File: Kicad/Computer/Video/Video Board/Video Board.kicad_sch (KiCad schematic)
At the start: 34 parts, among them IC1 74LVC2G04GW-Q100H, IC1 AP7365-33WG-7, IC1 SST39VF010-70-4I-NHE, IC27 74LVC1GX04GW,125, IC3 LD1117S50C

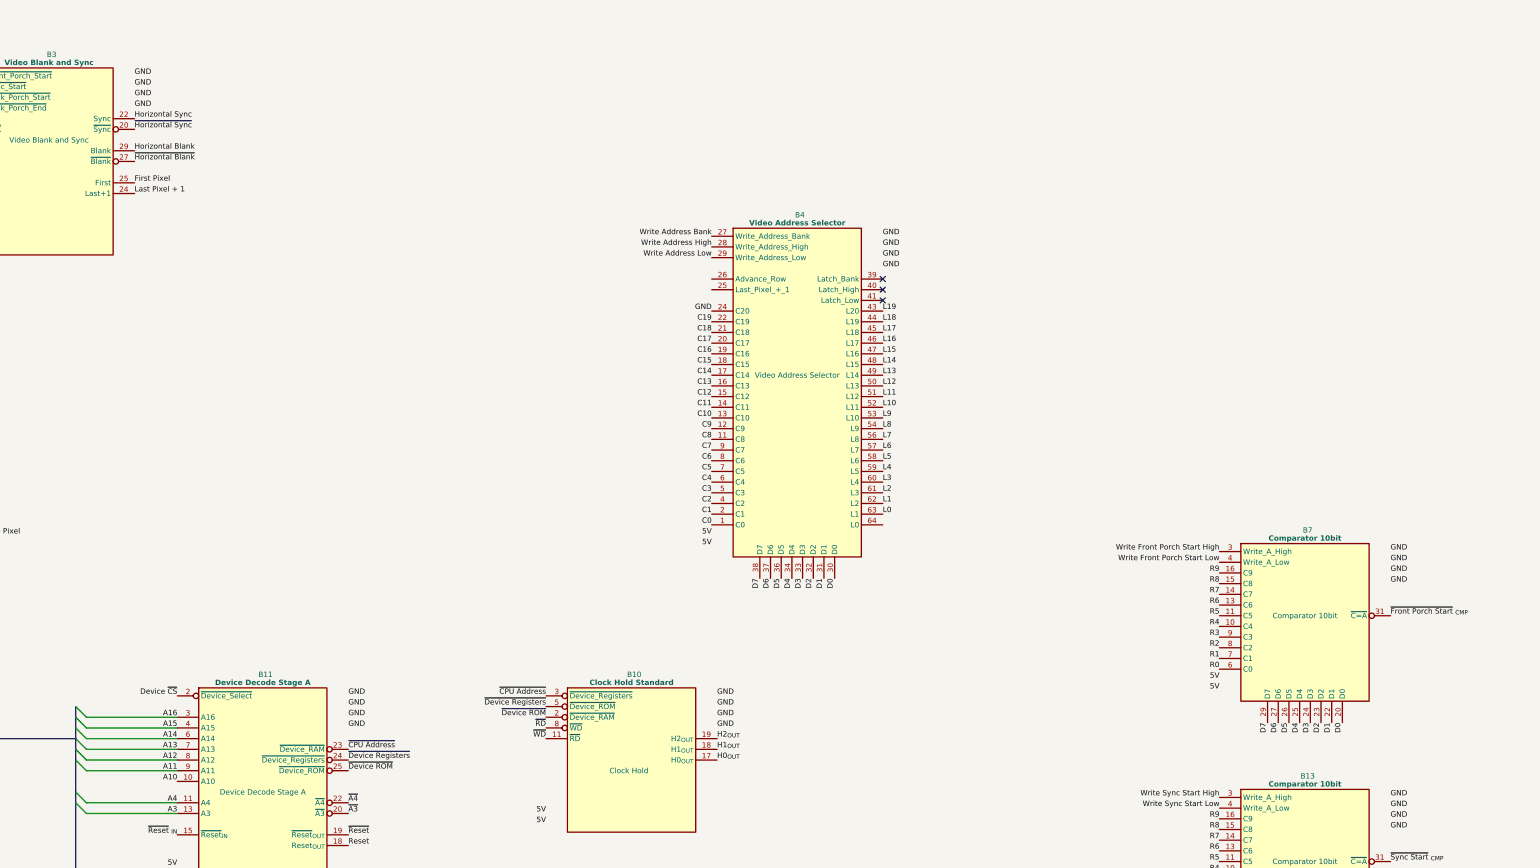
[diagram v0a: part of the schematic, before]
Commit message: Added Video Address Reader schematic and PCB.
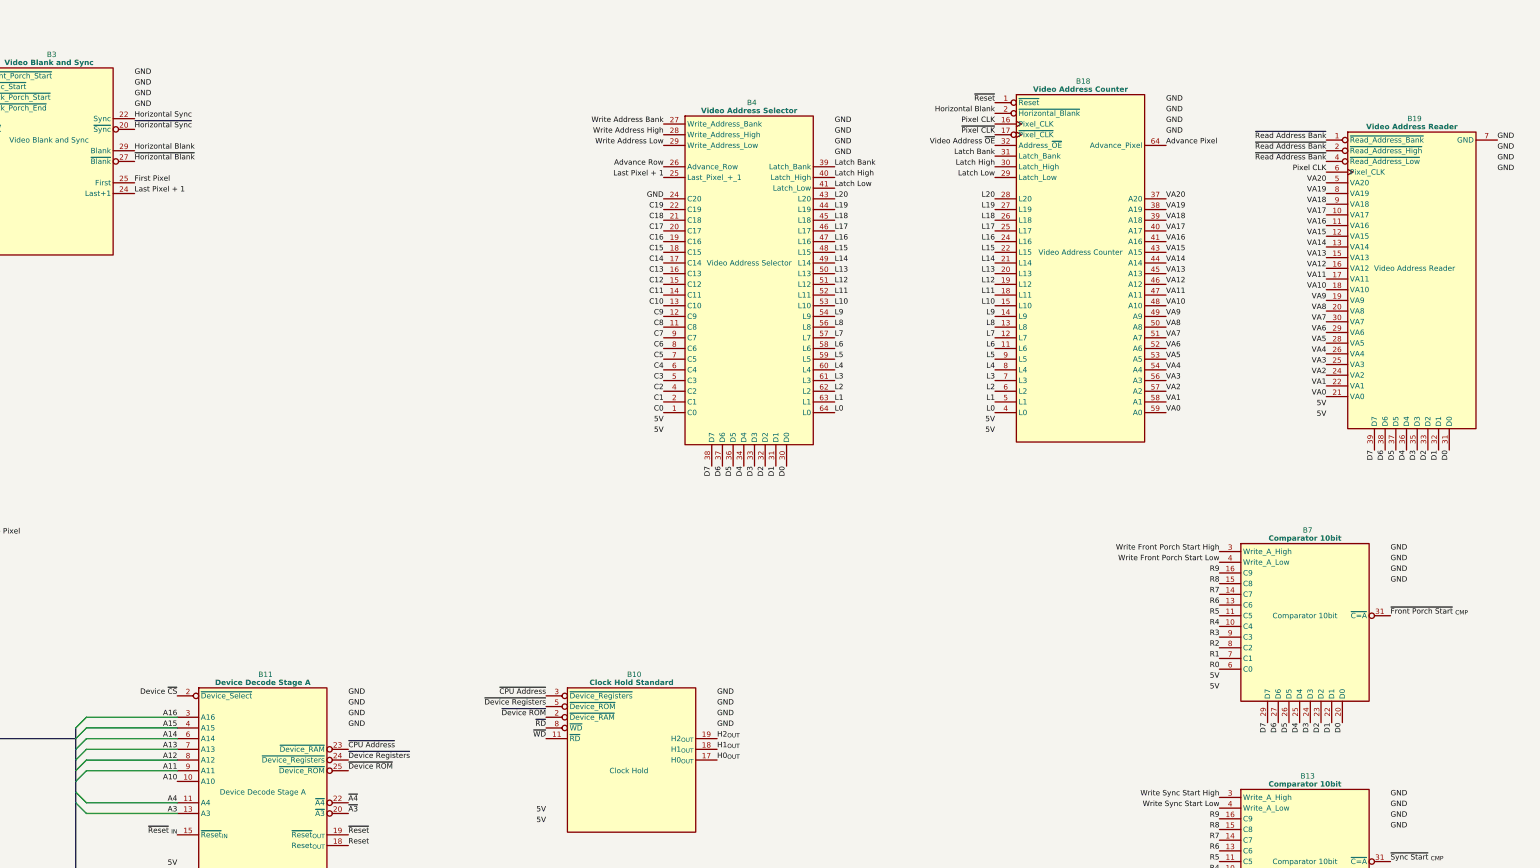
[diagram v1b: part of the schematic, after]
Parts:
- added B18: Video Address Counter, HCP65_Parts:HCP65_Video_Address_Counter, symbol HCP65:Video_Address_Counter
- added B19: Video Address Reader, HCP65_Parts:HCP65_Video_Address_Reader, symbol HCP65:Video_Address_Reader
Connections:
- net 5V: now also B18.3 (5V), B18.35 (5V), B19.23 (5V), B19.3 (5V)
- net Advance Pixel: now also B18.64 (Advance_Pixel)
- net D0: now also B19.31 (D0)
- net D1: now also B19.32 (D1)
- net D2: now also B19.33 (D2)
- net D3: now also B19.35 (D3)
- net D4: now also B19.36 (D4)
- net D5: now also B19.37 (D5)
- net D6: now also B19.38 (D6)
- net D7: now also B19.39 (D7)
- net GND: now also B18.10 (GND), B18.23 (GND), B18.42 (GND), B18.55 (GND), B19.14 (GND), B19.27 (GND), B19.34 (GND), B19.7 (GND)
- net Horizontal Blank: now also B18.2 (~{Horizontal_Blank})
- net L0: now also B4.64 (L0), B18.4 (L0); no longer B4.63 (L1)
- net L1: now also B4.63 (L1), B18.5 (L1); no longer B4.62 (L2)
- net L10: now also B4.53 (L10), B18.15 (L10); no longer B4.52 (L11)
- net L11: now also B4.52 (L11), B18.18 (L11); no longer B4.51 (L12)
- net L12: now also B4.51 (L12), B18.19 (L12); no longer B4.50 (L13)
- net L13: now also B4.50 (L13), B18.20 (L13); no longer B4.49 (L14)
- net L14: now also B4.49 (L14), B18.21 (L14); no longer B4.48 (L15)
- net L15: now also B4.48 (L15), B18.22 (L15); no longer B4.47 (L16)
- net L16: now also B4.47 (L16), B18.24 (L16); no longer B4.46 (L17)
- net L17: now also B4.46 (L17), B18.25 (L17); no longer B4.45 (L18)
- net L18: now also B4.45 (L18), B18.26 (L18); no longer B4.44 (L19)
- net L19: now also B4.44 (L19), B18.27 (L19); no longer B4.43 (L20)
- net L2: now also B4.62 (L2), B18.6 (L2); no longer B4.61 (L3)
- net L3: now also B4.61 (L3), B18.7 (L3); no longer B4.60 (L4)
- net L4: now also B4.60 (L4), B18.8 (L4); no longer B4.59 (L5)
- net L5: now also B4.59 (L5), B18.9 (L5); no longer B4.58 (L6)
- net L6: now also B4.58 (L6), B18.11 (L6); no longer B4.57 (L7)
- net L7: now also B4.57 (L7), B18.12 (L7); no longer B4.56 (L8)
- net L8: now also B4.56 (L8), B18.13 (L8); no longer B4.54 (L9)
- net L9: now also B4.54 (L9), B18.14 (L9); no longer B4.53 (L10)
- net Last Pixel + 1: now also B4.25 (Last_Pixel_+_1)
- net Pixel CLK: now also B18.16 (Pixel_CLK), B19.6 (Pixel_CLK)
- net ~{Pixel CLK}: now also B18.17 (~{Pixel_CLK})
- net ~{Reset}: now also B18.1 (~{Reset})
- net Advance Row: now reaches B4.26 (Advance_Row)
- net Latch Bank: now reaches B4.39 (Latch_Bank)
- net Latch Bank: now also B18.31 (Latch_Bank)
- net Latch High: now reaches B4.40 (Latch_High)
- net Latch High: now also B18.30 (Latch_High)
- net Latch Low: now reaches B4.41 (Latch_Low)
- net Latch Low: now also B18.29 (Latch_Low)
- new net L20: B18.28 (L20), B4.43 (L20)
- new net VA0: B18.59 (A0), B19.21 (VA0)
- new net VA1: B18.58 (A1), B19.22 (VA1)
- new net VA10: B18.48 (A10), B19.18 (VA10)
- new net VA11: B18.47 (A11), B19.17 (VA11)
- new net VA12: B18.46 (A12), B19.16 (VA12)
- new net VA13: B18.45 (A13), B19.15 (VA13)
- new net VA14: B18.44 (A14), B19.13 (VA14)
- new net VA15: B18.43 (A15), B19.12 (VA15)
- new net VA16: B18.41 (A16), B19.11 (VA16)
- new net VA17: B18.40 (A17), B19.10 (VA17)
- new net VA18: B18.39 (A18), B19.9 (VA18)
- new net VA19: B18.38 (A19), B19.8 (VA19)
- new net VA2: B18.57 (A2), B19.24 (VA2)
- new net VA20: B18.37 (A20), B19.5 (VA20)
- new net VA3: B18.56 (A3), B19.25 (VA3)
- new net VA4: B18.54 (A4), B19.26 (VA4)
- new net VA5: B18.53 (A5), B19.28 (VA5)
- new net VA6: B18.52 (A6), B19.29 (VA6)
- new net VA7: B18.51 (A7), B19.30 (VA7)
- new net VA8: B18.50 (A8), B19.20 (VA8)
- new net VA9: B18.49 (A9), B19.19 (VA9)
- new net Video Address ~{OE}: B18.32 (Address_~{OE})
- new net ~{Read Address Bank}: B19.1 (~{Read_Address_Bank}), B19.2 (~{Read_Address_High}), B19.4 (~{Read_Address_Low})
- no-connect marks 26 -> 23
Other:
- moved on the sheet: B4

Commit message: Began converting Video Board to new format.
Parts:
- removed C10, C11: 10µF, SamacSys_Parts:C_0805, symbol HCP65:C_0805
- removed C12 (x2): C_Polarized, Capacitor_THT:CP_Radial_D4.0mm_P2.00mm, symbol HCP65:C_Polarized
- removed H3, H4: MountingHole_Pad, HCP65_Parts:HCP65_MountingHole_M3_, symbol HCP65:MountingHole_Pad
- removed IC1: AP7365-33WG-7, SOT95P285X130-5N, symbol Diodes_Inc:AP7365-33WG-7
- removed IC3: LD1117S50C, LD1117S33C, symbol ST_Microelectronics:LD1117S50C
- removed J?: Conn_01x40_Pin, Connector_PinHeader_2.54mm:PinHeader_1x40_P2.54mm_Vertical, symbol Connector:Conn_01x40_Pin
- removed NT1: NetTie_2, NetTie:NetTie-2_SMD_Pad0.5mm, symbol Device:NetTie_2
- added C12 (x2): C_Polarized, Capacitor_THT:CP_Radial_D4.0mm_P2.00mm, symbol HCP65:C_Polarized
- added H16, H19, H8, H9: MountingHole_Pad, HCP65_Parts:HCP65_MountingHole_M3_, symbol HCP65:MountingHole_Pad
- added IC1: LD1117S50C, LD1117S33C, symbol ST_Microelectronics:LD1117S50C
- added J5: 395-098-520-350, SamacSys_Parts:98pin Edge Connector, symbol EDAC:395-098-520-350
- added LED1: LED, LED_THT:LED_D5.0mm, symbol HCP65:LED
- added R3: 10KΩ, SamacSys_Parts:R_0805, symbol HCP65:R_0805
- renumbered IC1 to IC2
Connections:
- net A0_{IN} is gone; now on net A0: B16.64 (A0)
- net A10_{IN} is gone; now on net A10: B16.53 (A10)
- net A11_{IN} is gone; now on net A11: B16.52 (A11)
- net A12_{IN} is gone; now on net A12: B16.51 (A12)
- net A13_{IN} is gone; now on net A13: B16.50 (A13)
- net A14_{IN} is gone; now on net A14: B16.49 (A14)
- net A15_{IN} is gone; now on net A15: B16.48 (A15)
- net A1_{IN} is gone; now on net A1: B16.63 (A1)
- net A2_{IN} is gone; now on net A2: B16.62 (A2)
- net A3_{IN} is gone; now on net A3: B16.61 (A3)
- net A4_{IN} is gone; now on net A4: B16.60 (A4)
- net A5_{IN} is gone; now on net A5: B16.59 (A5)
- net A6_{IN} is gone; now on net A6: B16.58 (A6)
- net A7_{IN} is gone; now on net A7: B16.57 (A7)
- net A8_{IN} is gone; now on net A8: B16.56 (A8)
- net A9_{IN} is gone; now on net A9: B16.54 (A9)
- net D0_{IN/OUT} is gone; now on net D0: B16.43 (D7)
- net D1_{IN/OUT} is gone; now on net D1: B16.41 (D6)
- net D2_{IN/OUT} is gone; now on net D2: B16.40 (D5)
- net D3_{IN/OUT} is gone; now on net D3: B16.39 (D4)
- net D4_{IN/OUT} is gone; now on net D4: B16.38 (D3)
- net D5_{IN/OUT} is gone; now on net D5: B16.37 (D2)
- net D6_{IN/OUT} is gone; now on net D6: B16.36 (D1)
- net D7_{IN/OUT} is gone; now on net D7: B16.34 (D0)
- net Device ~{CS} _{IN} is gone; now on net Device ~{CS}: B16.33 (Deivce_~{CS})
- net ~{WD}_{IN} is gone; now on net ~{WD}: B16.45 (~{WD})
- net 12V: now also C12.1, IC1.3 (15VIn), J5.B1
- net 3.3V: now also B10.24 (3.3V), B10.8 (H0_{REG})
- net 5V: now also C12.1, IC1.2 (5.0VOut), R3.2
- net A0: no longer B16.1 (A0)
- net A1: no longer B16.2 (A1)
- net A10: no longer B16.13 (A10)
- net A11: no longer B16.14 (A11)
- net A12: no longer B16.15 (A12)
- net A13: no longer B16.16 (A13)
- net A14: no longer B16.17 (A14)
- net A15: no longer B16.18 (A15)
- net A16: no longer B16.19 (A16)
- net A2: no longer B16.4 (A2)
- net A3: no longer B16.5 (A3)
- net A4: no longer B16.6 (A4)
- net A5: no longer B16.7 (A5)
- net A6: no longer B16.8 (A6)
- net A7: no longer B16.9 (A7)
- net A8: no longer B16.11 (A8)
- net A9: no longer B16.12 (A9)
- net D0: no longer B16.24 (D0)
- net D1: no longer B16.25 (D1)
- net D2: no longer B16.26 (D2)
- net D3: no longer B16.27 (D3)
- net D4: no longer B16.28 (D4)
- net D5: no longer B16.29 (D5)
- net D6: no longer B16.30 (D6)
- net D7: no longer B16.31 (D7)
- net Device ~{CS}: no longer B16.32 (Deivce_~{CS})
- net GND: now also B10.6 (H2_{REG}), B10.7 (H1_{REG}), B16.18 (A15_{IN}), B16.19 (A16_{IN}), C12.2, C12.2, H16.1 (GND), H19.1 (GND), H8.1 (GND), H9.1 (GND), IC1.1 (GND), J5.B10, J5.B17, J5.B2, J5.B24, J5.B31, J5.D18, J5.D9, LED1.2 (A); no longer B16.46 (S_{IN})
- net H0_{OUT}: now also B10.23 (N.C.); no longer B10.17 (H0_{OUT})
- net H1_{OUT}: now also B10.20 (N.C.); no longer B10.18 (H1_{OUT})
- net H2_{OUT}: now also B10.22 (N.C.); no longer B10.19 (H2_{OUT})
- net ~{CPU Address}: no longer B10.3 (~{Device_Registers})
- net ~{Device ROM}: now also B10.5 (~{Device_ROM}); no longer B10.2 (~{Device_RAM})
- net ~{Device Registers}: now also B10.3 (~{Device_Registers}); no longer B10.5 (~{Device_ROM})
- net ~{RD}: now also B10.10 (~{RD}), B16.46 (~{RD}); no longer B10.8 (~{WD}), B16.22 (~{RD})
- net ~{WD}: now also B10.12 (~{WD}); no longer B10.11 (~{RD}), B16.21 (~{WD})
- net ~{RD}_{D}: now reaches B16.20 (~{RD}_{IN})
- net ~{RD}_{D}: now also J5.B13
- net A16_{IN}: no longer names the net of B16.47 (A16)
- net ~{Enable} _{OUT} renamed ~{Enable}_{D}
- net ~{Enable}_{D}: now also J5.B22
- net ~{Interrupt} _{OUT} renamed ~{Interrupt}_{D}
- net ~{Interrupt}_{D}: now also J5.B19
- net ~{RD}_{IN}: no longer names the net of B16.44 (S)
- net ~{Reset} _{IN} renamed ~{Reset}_{D}
- net ~{Reset}_{D}: now also J5.B20
- new net: LED1.1 (K), R3.1
- new net A0_{D}: B16.1 (A0_{IN}), J5.A4
- new net A0_{M}: J5.D17
- new net A10_{D}: B16.13 (A10_{IN}), J5.A14
- new net A10_{M}: J5.C14
- new net A11_{D}: B16.14 (A11_{IN}), J5.A15
- new net A11_{M}: J5.C13
- new net A12_{D}: B16.15 (A12_{IN}), J5.A16
- new net A12_{M}: J5.C12
- new net A13_{D}: B16.16 (A13_{IN}), J5.A17
- new net A13_{M}: J5.C11
- new net A14_{D}: B16.17 (A14_{IN}), J5.A18
- new net A14_{M}: J5.C10
- new net A15_{D}: J5.A19
- new net A15_{M}: J5.C9
- new net A16_{D}: J5.A20
- new net A16_{M}: J5.C8
- new net A17_{M}: J5.C7
- new net A18_{M}: J5.C6
- new net A19_{M}: J5.C5
- new net A1_{D}: B16.2 (A1_{IN}), J5.A5
- new net A1_{M}: J5.D16
- new net A20_{M}: J5.C4
- new net A21_{M}: J5.C3
- new net A22_{M}: J5.C2
- new net A23_{M}: J5.C1
- new net A2_{D}: B16.4 (A2_{IN}), J5.A6
- new net A2_{M}: J5.D15
- new net A3_{D}: B16.5 (A3_{IN}), J5.A7
- new net A3_{M}: J5.D14
- new net A4_{D}: B16.6 (A4_{IN}), J5.A8
- new net A4_{M}: J5.D13
- new net A5_{D}: B16.7 (A5_{IN}), J5.A9
- new net A5_{M}: J5.D12
- new net A6_{D}: B16.8 (A6_{IN}), J5.A10
- new net A6_{M}: J5.C18
- new net A7_{D}: B16.9 (A7_{IN}), J5.A11
- new net A7_{M}: J5.C17
- new net A8_{D}: B16.11 (A8_{IN}), J5.A12
- new net A8_{M}: J5.C16
- new net A9_{D}: B16.12 (A9_{IN}), J5.A13
- new net A9_{M}: J5.C15
- new net CLK_{D}: B16.22 (S_{IN}), J5.B15
- new net D0_{D}: B16.31 (D0_{IN/OUT}), J5.A28
- new net D0_{M}: J5.D8
- new net D1_{D}: B16.30 (D1_{IN/OUT}), J5.A27
- new net D1_{M}: J5.D7
- new net D2_{D}: B16.29 (D2_{IN/OUT}), J5.A26
- new net D2_{M}: J5.D6
- new net D3_{D}: B16.28 (D3_{IN/OUT}), J5.A25
- new net D3_{M}: J5.D5
- new net D4_{D}: B16.27 (D4_{IN/OUT}), J5.A24
- new net D4_{M}: J5.D4
- new net D5_{D}: B16.26 (D5_{IN/OUT}), J5.A23
- new net D5_{M}: J5.D3
- new net D6_{D}: B16.25 (D6_{IN/OUT}), J5.A22
- new net D6_{M}: J5.D2
- new net D7_{D}: B16.24 (D7_{IN/OUT}), J5.A21
- new net D7_{M}: J5.D1
- new net H0_{D}: B10.17 (H0_{OUT}), J5.A31
- new net H1_{D}: B10.18 (H1_{OUT}), J5.A30
- new net H2_{D}: B10.19 (H2_{OUT}), J5.A29
- new net ~{CLK}_{D}: J5.B16
- new net ~{Device RAM}: B10.2 (~{Device_RAM})
- new net ~{Device Select}: B10.11 (~{Device_Select})
- new net ~{Memory A}: J5.B29
- new net ~{Memory B}: J5.B30
- new net ~{RD}_{M}: J5.D10
- new net ~{Reset}_{System}: J5.A1
- new net ~{Select}_{D}: B16.32 (Deivce_~{CS}_{IN}), J5.B21
- new net ~{WD}_{D}: B16.21 (~{WD}_{IN}), J5.B14
- new net ~{WD}_{M}: J5.D11
- no-connect marks 23 -> 39

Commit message: Still converting the Video Board.
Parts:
- added B20: Video Blank and Sync, HCP65_Parts:HCP65_Video_Blank_and_Sync, symbol HCP65:Video_Blank_and_Sync
- added B21: Video Counter 12bit, HCP65_Parts:HCP65_Video_Counter_12bit, symbol HCP65:Video_Counter_12bit
- added B22: Video Pixel Doubler, HCP65_Parts:HCP65_Video_Pixel_Doubler, symbol HCP65:Video_Pixel_Doubler
- added B23, B25: Device Decode Stage B, HCP65_Parts:HCP65_Device_Decode_Stage_B, symbol HCP65:Device_Decode_Stage_B
- added B24: D-type Flip Flop 24bit, symbol HCP65:D_Flip_Flop_24bit
- added C23 (x3): 1μF, SamacSys_Parts:C_0805, symbol HCP65:C_0805
- added IC100, IC101: 74LVC1G157GV,125, 74LVC1G157GV125, symbol Nexperia:74LVC1G157GV,125
- added IC13: 74LVC574APW,118, SOP65P640X110-20N, symbol Nexperia:74LVC574APW,118
- C12: footprint Capacitor_THT:CP_Radial_D4.0mm_P2.00mm -> (none)
- LED1: footprint LED_THT:LED_D5.0mm -> (none)
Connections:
- net Device ~{CS} is gone; now on net ~{Device Select}: B11.2 (~{Device_Select}), B16.33 (Deivce_~{CS})
- net Write Front Porch Start High is gone; now on net Write Vertical Front Porch Start High: B7.3 (Write_A_High)
- net Write Front Porch Start Low is gone; now on net Write Vertical Front Porch Start Low: B7.4 (Write_A_Low)
- net Write Sync Start High is gone; now on net Write Vertical Sync Start High: B13.3 (Write_A_High)
- net Write Sync Start Low is gone; now on net Write Vertical Sync Start Low: B13.4 (Write_A_Low)
- net 3.3V: now also B21.16 (IR0), B21.40 (~{CLK}), C23.1, C23.1, C23.1, IC100.5 (3V), IC101.5 (3V), IC13.20 (3V)
- net 5V: now also B20.1 (5V), B20.17 (5V), B21.23 (5V), B21.3 (5V), B22.1 (5V), B22.17 (5V), B23.1 (5V), B23.17 (5V), B24.3 (5V), B24.31 (5V), B25.1 (5V), B25.17 (5V)
- net A0: now also B23.13 (A0), B25.13 (A0)
- net A1: now also B23.11 (A1), B25.11 (A1)
- net A16: now also B16.47 (A16)
- net A2: now also B23.10 (A2), B25.10 (A2)
- net A3: now also B23.8 (~{E2})
- net A4: now also B23.9 (E3), B25.9 (E3)
- net Advance Row: now also B22.31 (Selected_Pattern)
- net C0: now also B18.59 (C0), B19.21 (C0), B4.24 (C0), B24.28 (IN0); no longer B4.1 (C0)
- net C1: now also B18.58 (C1), B19.22 (C1), B4.22 (C1), B24.27 (IN1); no longer B4.2 (C1)
- net C10: now also B18.48 (C10), B19.18 (C10), B24.17 (IN10)
- net C11: now also B18.47 (C11), B19.17 (C11), B4.12 (C11), B24.16 (IN11); no longer B4.14 (C11)
- net C12: now also B18.46 (C12), B19.16 (C12), B4.11 (C12), B24.15 (IN12); no longer B4.15 (C12)
- net C13: now also B18.45 (C13), B19.15 (C13), B4.9 (C13), B24.14 (IN13); no longer B4.16 (C13)
- net C14: now also B18.44 (C14), B19.13 (C14), B4.8 (C14), B24.13 (IN14); no longer B4.17 (C14)
- net C15: now also B18.43 (C15), B19.12 (C15), B4.7 (C15), B24.12 (IN15); no longer B4.18 (C15)
- net C16: now also B18.41 (C16), B19.11 (C16), B4.6 (C16), B24.11 (IN16); no longer B4.19 (C16)
- net C17: now also B18.40 (C17), B19.10 (C17), B4.5 (C17), B24.9 (IN17); no longer B4.20 (C17)
- net C18: now also B18.39 (C18), B19.9 (C18), B4.4 (C18), B24.8 (IN18); no longer B4.21 (C18)
- net C19: now also B18.38 (C19), B19.8 (C19), B4.2 (C19), B24.7 (IN19); no longer B4.22 (C19)
- net C2: now also B18.57 (C2), B19.24 (C2), B4.21 (C2), B24.26 (IN2); no longer B4.4 (C2)
- net C3: now also B18.56 (C3), B19.25 (C3), B4.20 (C3), B24.25 (IN3); no longer B4.5 (C3)
- net C4: now also B18.54 (C4), B19.26 (C4), B4.19 (C4), B24.24 (IN4); no longer B4.6 (C4)
- net C5: now also B18.53 (C5), B19.28 (C5), B4.18 (C5), B24.23 (IN5); no longer B4.7 (C5)
- net C6: now also B18.52 (C6), B19.29 (C6), B4.17 (C6), B24.22 (IN6); no longer B4.8 (C6)
- net C7: now also B18.51 (C7), B19.30 (C7), B4.16 (C7), B24.21 (IN7); no longer B4.9 (C7)
- net C8: now also B18.50 (C8), B19.20 (C8), B4.15 (C8), B24.19 (IN8); no longer B4.11 (C8)
- net C9: now also B18.49 (C9), B19.19 (C9), B4.14 (C9), B24.18 (IN9); no longer B4.12 (C9)
- net D0: now also B21.15 (D0), B22.16 (D0)
- net D1: now also B21.13 (D1), B22.15 (D1)
- net D2: now also B21.12 (D2), B22.14 (D2)
- net D3: now also B21.11 (D3), B22.13 (D3)
- net D4: now also B21.10 (D4), B22.11 (D4)
- net D5: now also B21.9 (D5), B22.10 (D5)
- net D6: now also B21.8 (D6), B22.9 (D6)
- net D7: now also B21.6 (D7), B22.8 (D7)
- net First Pixel: now also B21.19 (CLK), B22.4 (CLK), IC13.5 (D3)
- net GND: now also B20.12 (GND), B20.21 (GND), B20.28 (GND), B20.5 (GND), B21.14 (GND), B21.17 (IR1), B21.27 (GND), B21.34 (GND), B21.7 (GND), B22.12 (GND), B22.21 (GND), B22.28 (GND), B22.5 (GND), B23.12 (GND), B23.21 (GND), B23.28 (GND), B23.5 (GND), B24.10 (GND), B24.2 (IN23), B24.20 (GND), B24.37 (GND), B24.4 (IN22), B24.47 (GND), B24.5 (IN21), B25.12 (GND), B25.21 (GND), B25.28 (GND), B25.5 (GND), C23.2, C23.2, C23.2, IC100.2 (GND), IC101.2 (GND), IC13.1 (~{OE}), IC13.10 (GND); no longer B4.24 (C20)
- net Horizontal Blank: now also IC13.8 (D6)
- net Horizontal Sync: now also IC101.3 (I0)
- net L0: now also B4.43 (L0); no longer B4.64 (L0)
- net L1: now also B4.44 (L1); no longer B4.63 (L1)
- net L11: now also B4.54 (L11); no longer B4.52 (L11)
- net L12: now also B4.56 (L12); no longer B4.51 (L12)
- net L13: now also B4.57 (L13); no longer B4.50 (L13)
- net L14: now also B4.58 (L14); no longer B4.49 (L14)
- net L15: now also B4.59 (L15); no longer B4.48 (L15)
- net L16: now also B4.60 (L16); no longer B4.47 (L16)
- net L17: now also B4.61 (L17); no longer B4.46 (L17)
- net L18: now also B4.62 (L18); no longer B4.45 (L18)
- net L19: now also B4.63 (L19); no longer B4.44 (L19)
- net L2: now also B4.45 (L2); no longer B4.62 (L2)
- net L20: now also B4.64 (L20); no longer B4.43 (L20)
- net L3: now also B4.46 (L3); no longer B4.61 (L3)
- net L4: now also B4.47 (L4); no longer B4.60 (L4)
- net L5: now also B4.48 (L5); no longer B4.59 (L5)
- net L6: now also B4.49 (L6); no longer B4.58 (L6)
- net L7: now also B4.50 (L7); no longer B4.57 (L7)
- net L8: now also B4.51 (L8); no longer B4.56 (L8)
- net L9: now also B4.52 (L9); no longer B4.54 (L9)
- net Last Pixel + 1: now also IC13.4 (D2)
- net R0: now also B21.38 (R0)
- net R1: now also B21.37 (R1)
- net R2: now also B21.36 (R2)
- net R3: now also B21.35 (R3)
- net R4: now also B21.33 (R4)
- net R5: now also B21.32 (R5)
- net R6: now also B21.31 (R6)
- net R7: now also B21.30 (R7)
- net R8: now also B21.29 (R8)
- net R9: now also B21.28 (R9)
- net Read Flags: now also B15.32 (Y0_{R})
- net Read Horizontal High: now also B15.2 (Y7_{R}); no longer B15.31 (Y1_{R})
- net Read Horizontal Low: now also B15.3 (Y6_{R}); no longer B15.32 (Y0_{R})
- net VA0: now also B24.29 (OUT0); no longer B18.59 (A0), B19.21 (VA0)
- net VA1: now also B24.30 (OUT1); no longer B18.58 (A1), B19.22 (VA1)
- net VA10: now also B24.41 (OUT10); no longer B18.48 (A10), B19.18 (VA10)
- net VA11: now also B24.42 (OUT11); no longer B18.47 (A11), B19.17 (VA11)
- net VA12: now also B24.43 (OUT12); no longer B18.46 (A12), B19.16 (VA12)
- net VA13: now also B24.44 (OUT13); no longer B18.45 (A13), B19.15 (VA13)
- net VA14: now also B24.45 (OUT14); no longer B18.44 (A14), B19.13 (VA14)
- net VA15: now also B24.46 (OUT15); no longer B18.43 (A15), B19.12 (VA15)
- net VA16: now also B24.48 (OUT16); no longer B18.41 (A16), B19.11 (VA16)
- net VA17: now also B24.49 (OUT17); no longer B18.40 (A17), B19.10 (VA17)
- net VA18: now also B24.50 (OUT18); no longer B18.39 (A18), B19.9 (VA18)
- net VA19: now also B24.51 (OUT19); no longer B18.38 (A19), B19.8 (VA19)
- net VA2: now also B24.32 (OUT2); no longer B18.57 (A2), B19.24 (VA2)
- net VA20: now also B24.52 (OUT20); no longer B18.37 (A20), B19.5 (VA20)
- net VA3: now also B24.33 (OUT3); no longer B18.56 (A3), B19.25 (VA3)
- net VA4: now also B24.34 (OUT4); no longer B18.54 (A4), B19.26 (VA4)
- net VA5: now also B24.35 (OUT5); no longer B18.53 (A5), B19.28 (VA5)
- net VA6: now also B24.36 (OUT6); no longer B18.52 (A6), B19.29 (VA6)
- net VA7: now also B24.38 (OUT7); no longer B18.51 (A7), B19.30 (VA7)
- net VA8: now also B24.39 (OUT8); no longer B18.50 (A8), B19.20 (VA8)
- net VA9: now also B24.40 (OUT9); no longer B18.49 (A9), B19.19 (VA9)
- net Video Address ~{OE}: now also B24.1 (~{OE}); no longer B18.32 (Address_~{OE})
- net Write Address Bank: now also B15.23 (Y4_{W})
- net Write Address High: now also B15.24 (Y3_{W})
- net Write Address Low: now also B15.25 (Y2_{W})
- net Write Clear Interrupt: now also B15.26 (Y1_{W})
- net Write Flags: now also B15.27 (Y0_{W})
- net ~{A3}: now also B25.8 (~{E2})
- net ~{Device Registers}: now also B23.4 (~{Device_Registers}), B25.4 (~{Device_Registers})
- net ~{Horizontal Sync}: now also IC101.1 (I1)
- net ~{Pixel CLK}: now also B24.56 (CLK), IC13.11 (CP)
- net ~{RD}: now also B23.15 (~{RD}), B25.15 (~{RD})
- net ~{Reset}: now also B21.1 (~{Reset}), B22.2 (~{Reset})
- net ~{WD}: now also B23.16 (~{WD}), B25.16 (~{WD})
- net Vertical Sync Polarity: now reaches B8.18 (F0)
- net Vertical Sync Polarity: now also IC100.6 (S)
- net Horizontal Sync Polarity: now reaches B8.19 (F1)
- net Horizontal Sync Polarity: now also IC101.6 (S)
- net Write Vertical Sync Start High: now reaches B9.19 (Y7_{W})
- net Write Vertical Sync Start Low: now reaches B9.20 (Y6_{W})
- net Write Vertical Front Porch Start High: now reaches B9.22 (Y5_{W})
- net Write Vertical Front Porch Start Low: now reaches B9.23 (Y4_{W})
- net Write Horizontal Shift Pattern High: now reaches B9.24 (Y3_{W})
- net Write Horizontal Shift Pattern High: now also B1.7 (Write_Pattern_High)
- net Write Horizontal Shift Pattern Low: now reaches B9.25 (Y2_{W})
- net Write Horizontal Shift Pattern Low: now also B1.6 (Write_Pattern_Low)
- net Write Horizontal Back Porch End: now reaches B9.26 (Y1_{W})
- net Write Horizontal Back Porch End: now also B6.33 (Write_B)
- net Write Horizontal Back Porch Start: now reaches B9.27 (Y0_{W})
- net Write Horizontal Back Porch Start: now also B6.26 (Write_A)
- net Read Vertical High: now reaches B9.6 (Y5_{R})
- net Read Vertical High: now also B21.4 (Read_Row_Position_High)
- net Read Vertical Low: now reaches B9.7 (Y4_{R})
- net Read Vertical Low: now also B21.5 (Read_Row_Position_Low)
- net Write Horiztonal Sync Start: now reaches B15.19 (Y7_{W})
- net Write Horiztonal Sync Start: now also B5.33 (Write_B)
- net Write Horizontal Front Porch Start: now reaches B15.20 (Y6_{W})
- net Write Horizontal Front Porch Start: now also B5.26 (Write_A)
- net Read Address High: now reaches B15.29 (Y3_{R})
- net Read Address High: now also B19.2 (Read_Address_High)
- net Read Address Low: now reaches B15.30 (Y2_{R})
- net Read Address Low: now also B19.4 (Read_Address_Low)
- net Read Address Bank: now reaches B15.7 (Y4_{R})
- net Read Address Bank: now also B19.1 (Read_Address_Bank)
- net H0_{OUT}: no longer names the net of B10.23 (N.C.)
- net H1_{OUT}: no longer names the net of B10.20 (N.C.)
- net H2_{OUT}: no longer names the net of B10.22 (N.C.)
- net Latch Bank renamed Latch Address Bank
- net Latch High renamed Latch Address High
- net Latch Low renamed Latch Address Low
- removed net Write Back Porch End: B15.24 (Y3_{W}), B6.33 (Write_B)
- net Write Back Porch End High renamed Write Vertical Back Porch End High
- net Write Vertical Back Porch End High: now also B23.24 (Y3_{W})
- net Write Back Porch End Low renamed Write Vertical Back Porch End Low
- net Write Vertical Back Porch End Low: now also B23.25 (Y2_{W})
- removed net Write Back Porch Start: B15.25 (Y2_{W}), B6.26 (Write_A)
- net Write Back Porch Start High renamed Write Vertical Back Porch Start High
- net Write Vertical Back Porch Start High: now also B23.26 (Y1_{W})
- net Write Back Porch Start Low renamed Write Vertical Back Porch Start Low
- net Write Vertical Back Porch Start Low: now also B23.27 (Y0_{W})
- removed net Write Front Porch Start: B15.27 (Y0_{W}), B5.26 (Write_A)
- net Write Interrupt High renamed Write Vertical Interrupt High
- net Write Vertical Interrupt High: now also B23.22 (Y5_{W})
- net Write Interrupt Low renamed Write Vertical Interrupt Low
- net Write Vertical Interrupt Low: now also B23.23 (Y4_{W})
- removed net Write Shift Pattern High: B1.7 (Write_Pattern_High), B15.23 (Y4_{W})
- net Write Shift Pattern Low: no longer names the net of B15.22 (Y5_{W})
- net Write Shift Pattern Low: no longer B1.6 (Write_Pattern_Low)
- removed net Write Sync Start: B15.26 (Y1_{W}), B5.33 (Write_B)
- net ~{Back Porch End} _{CMP} renamed ~{Horizontal Back Porch End} _{CMP}
- net ~{Horizontal Back Porch End} _{CMP}: no longer B12.31 (~{C=A})
- net ~{Back Porch Start} _{CMP} renamed ~{Horizontal Back Porch Start} _{CMP}
- net ~{Horizontal Back Porch Start} _{CMP}: no longer B14.31 (~{C=A})
- net ~{Front Porch Start} _{CMP} renamed ~{Horizontal Front Porch Start} _{CMP}
- net ~{Horizontal Front Porch Start} _{CMP}: no longer B7.31 (~{C=A})
- net ~{Interrupt} _{CMP} renamed ~{Vertical Interrupt} _{CMP}
- removed net ~{Read Address Bank}: B19.1 (~{Read_Address_Bank}), B19.2 (~{Read_Address_High}), B19.4 (~{Read_Address_Low})
- net ~{Sync Start} _{CMP} renamed ~{Horizontal Sync Start} _{CMP}
- net ~{Horizontal Sync Start} _{CMP}: no longer B13.31 (~{C=A})
- new net C20: B18.37 (C20), B19.5 (C20), B24.6 (IN20), B4.1 (C20)
- new net First Pixel _{HALF CYCLE}: B20.8 (~{CLK}), IC13.16 (Q3)
- new net First Row: B20.25 (First), IC13.3 (D1)
- new net First Row _{HALF CYCLE}: IC13.18 (Q1)
- new net Horizontal Blank _{HALF CYCLE}: IC13.13 (Q6)
- new net Horizontal Sync _{HALF CYCLE}: IC13.12 (Q7)
- new net Horizontal Sync _{SEL}: IC101.4 (Y), IC13.9 (D7)
- new net Last Pixel + 1 _{HALF CYCLE}: IC13.17 (Q2)
- new net Last Row + 1: B20.24 (Last+1), IC13.2 (D0)
- new net Last Row + 1 _{HALF CYCLE}: IC13.19 (Q0)
- new net Vertical Blank: B20.29 (Blank), IC13.6 (D4)
- new net Vertical Blank _{HALF CYCLE}: IC13.15 (Q4)
- new net Vertical Sync: B20.22 (Sync), IC100.3 (I0)
- new net Vertical Sync _{HALF CYCLE}: IC13.14 (Q5)
- new net Vertical Sync _{SEL}: IC100.4 (Y), IC13.7 (D5)
- new net Write Vertical Shift Pattern High: B22.7 (Write_Pattern_High), B23.19 (Y7_{W})
- new net Write Vertical Shift Pattern Low: B22.6 (Write_Pattern_Low), B23.20 (Y6_{W})
- new net ~{Front Porch Start}: B20.31 (~{Front_Porch_Start})
- new net ~{Vertical Back Porch End}: B20.18 (~{Back_Porch_End}), B21.2 (~{Load})
- new net ~{Vertical Back Porch End} _{CMP}: B12.31 (~{C=A}), B20.13 (~{Back_Porch_End})
- new net ~{Vertical Back Porch Start} _{CMP}: B14.31 (~{C=A}), B20.11 (~{Back_Porch_Start})
- new net ~{Vertical Blank}: B20.27 (~{Blank}), B22.3 (Enable_Pattern)
- new net ~{Vertical Front Porch Start} _{CMP}: B20.4 (~{Front_Porch_Start}), B7.31 (~{C=A})
- new net ~{Vertical Sync Start} _{CMP}: B13.31 (~{C=A}), B20.6 (~{Sync_Start})
- new net ~{Vertical Sync}: B20.20 (~{Sync}), IC100.1 (I1)
- no-connect marks 39 -> 78
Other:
- moved on the sheet: B1, B10, B11, B12, B13, B14, B15, B16, B17, B2, B4, B7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
